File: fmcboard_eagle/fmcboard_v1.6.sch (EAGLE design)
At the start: 231 parts, among them IC1 OPA699ID, IC10 LM358, IC11 7805DT, IC12 SN74AUC2G66DCTR, IC13 SN74AUC2G66DCTR, IC14 SN74AUC2G66DCTR, IC15 SN74AUC2G66DCTR, IC16 DAC7578SPWR, IC17 SN74AUC2G66DCTR, IC18 SN74AUC2G66DCTR, IC19 SN74AUC2G66DCTR, IC2 DAC7578SPWR, IC20 SN74AUC2G66DCTR, IC21 74AUP2GU04GW, IC22 74AUP2GU04GW, IC23 74AUP2GU04GW, IC24 74AUP2GU04GW, IC25 MC7905ACD2TR4G, IC26 AMS1117-1.8, IC29 LM337KVURG3, IC3 LTC6229IMS8E#TRPBF, IC4 OPA695IDR, IC5 LTC6229IMS8E#TRPBF, IC6 OPA695IDR, IC7 OPA699ID, IC8 LM358, IC9 LM358, J1 8pin, J11 4p-2.54, J12 4p-2.54, J13 4p-2.54, J2 ASP-134604-01, J3 4p-2.54, J4 4p-2.54, J5 4p-2.54, J6 4p-2.54, J7 4p-2.54, J8 4p-2.54, J9 8pin, U1 TXS0108EPWR

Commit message: v1.64
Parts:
- R13, R3, R71, R72, R86, R88, R89: LCSC (none) -> C17415
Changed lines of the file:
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@@
 <part name="SUPPLY113" library="supply2" library_urn="urn:adsk.eagle:library:372" deviceset="GND" device=""/>
 <part name="SUPPLY114" library="supply2" library_urn="urn:adsk.eagle:library:372" deviceset="GND" device=""/>
-<part name="R3" library="rcl" library_urn="urn:adsk.eagle:library:334" deviceset="R-US_" device="R0805" package3d_urn="urn:adsk.eagle:package:23553/2" value="10"/>
+<part name="R3" library="rcl" library_urn="urn:adsk.eagle:library:334" deviceset="R-US_" device="R0805" package3d_urn="urn:adsk.eagle:package:23553/2" value="10">
+<spice>
+<pinmapping spiceprefix="R">
+<pinmap gate="G$1" pin="1" pinorder="1"/>
+<pinmap gate="G$1" pin="2" pinorder="2"/>
+</pinmapping>
+</spice>
+<attribute name="LCSC" value="C17415"/>
+</part>
 <part name="SUPPLY18" library="supply2" library_urn="urn:adsk.eagle:library:372" deviceset="GND" device=""/>
-<part name="R13" library="rcl" library_urn="urn:adsk.eagle:library:334" deviceset="R-US_" device="R0805" package3d_urn="urn:adsk.eagle:package:23553/2" value="10"/>
+<part name="R13" library="rcl" library_urn="urn:adsk.eagle:library:334" deviceset="R-US_" device="R0805" package3d_urn="urn:adsk.eagle:package:23553/2" value="10">
+<spice>
+<pinmapping spiceprefix="R">
+<pinmap gate="G$1" pin="1" pinorder="1"/>
+<pinmap gate="G$1" pin="2" pinorder="2"/>
+</pinmapping>
+</spice>
+<attribute name="LCSC" value="C17415"/>
+</part>
 <part name="SUPPLY21" library="supply2" library_urn="urn:adsk.eagle:library:372" deviceset="GND" device=""/>
 <part name="R35" library="rcl" library_urn="urn:adsk.eagle:library:334" deviceset="R-US_" device="R0805" package3d_urn="urn:adsk.eagle:package:23553/2" value="1k"/>
@@
 <part name="J11" library="Seeed-Connector" library_urn="urn:adsk.eagle:library:478" deviceset="DIP-BLACK-FEMALE-HEADER-VERT(4P-2.54)" device="" package3d_urn="urn:adsk.eagle:package:33137/1" value="4p-2.54"/>
 <part name="J13" library="Seeed-Connector" library_urn="urn:adsk.eagle:library:478" deviceset="DIP-BLACK-FEMALE-HEADER-VERT(4P-2.54)" device="" package3d_urn="urn:adsk.eagle:package:33137/1" value="4p-2.54"/>
-<part name="R71" library="rcl" library_urn="urn:adsk.eagle:library:334" deviceset="R-US_" device="R0805" package3d_urn="urn:adsk.eagle:package:23553/2" value="10"/>
-<part name="R72" library="rcl" library_urn="urn:adsk.eagle:library:334" deviceset="R-US_" device="R0805" package3d_urn="urn:adsk.eagle:package:23553/2" value="10"/>
-<part name="R86" library="rcl" library_urn="urn:adsk.eagle:library:334" deviceset="R-US_" device="R0805" package3d_urn="urn:adsk.eagle:package:23553/2" value="10"/>
-<part name="R88" library="rcl" library_urn="urn:adsk.eagle:library:334" deviceset="R-US_" device="R0805" package3d_urn="urn:adsk.eagle:package:23553/2" value="10"/>
+<part name="R71" library="rcl" library_urn="urn:adsk.eagle:library:334" deviceset="R-US_" device="R0805" package3d_urn="urn:adsk.eagle:package:23553/2" value="10">
+<spice>
+<pinmapping spiceprefix="R">
+<pinmap gate="G$1" pin="1" pinorder="1"/>
+<pinmap gate="G$1" pin="2" pinorder="2"/>
+</pinmapping>
+</spice>
+<attribute name="LCSC" value="C17415"/>
+</part>
+<part name="R72" library="rcl" library_urn="urn:adsk.eagle:library:334" deviceset="R-US_" device="R0805" package3d_urn="urn:adsk.eagle:package:23553/2" value="10">
+<spice>
+<pinmapping spiceprefix="R">
+<pinmap gate="G$1" pin="1" pinorder="1"/>
+<pinmap gate="G$1" pin="2" pinorder="2"/>
+</pinmapping>
+</spice>
+<attribute name="LCSC" value="C17415"/>
+</part>
+<part name="R86" library="rcl" library_urn="urn:adsk.eagle:library:334" deviceset="R-US_" device="R0805" package3d_urn="urn:adsk.eagle:package:23553/2" value="10">
+<spice>
+<pinmapping spiceprefix="R">
+<pinmap gate="G$1" pin="1" pinorder="1"/>
+<pinmap gate="G$1" pin="2" pinorder="2"/>
+</pinmapping>
+</spice>
+<attribute name="LCSC" value="C17415"/>
+</part>
+<part name="R88" library="rcl" library_urn="urn:adsk.eagle:library:334" deviceset="R-US_" device="R0805" package3d_urn="urn:adsk.eagle:package:23553/2" value="10">
+<spice>
+<pinmapping spiceprefix="R">
+<pinmap gate="G$1" pin="1" pinorder="1"/>
+<pinmap gate="G$1" pin="2" pinorder="2"/>
+</pinmapping>
+</spice>
+<attribute name="LCSC" value="C17415"/>
+</part>
 <part name="J5" library="Seeed-Connector" library_urn="urn:adsk.eagle:library:478" deviceset="DIP-BLACK-FEMALE-HEADER-VERT(4P-2.54)" device="" package3d_urn="urn:adsk.eagle:package:33137/1" value="4p-2.54"/>
-<part name="R89" library="rcl" library_urn="urn:adsk.eagle:library:334" deviceset="R-US_" device="R0805" package3d_urn="urn:adsk.eagle:package:23553/2" value="10"/>
+<part name="R89" library="rcl" library_urn="urn:adsk.eagle:library:334" deviceset="R-US_" device="R0805" package3d_urn="urn:adsk.eagle:package:23553/2" value="10">
+<spice>
+<pinmapping spiceprefix="R">
+<pinmap gate="G$1" pin="1" pinorder="1"/>
+<pinmap gate="G$1" pin="2" pinorder="2"/>
+</pinmapping>
+</spice>
+<attribute name="LCSC" value="C17415"/>
+</part>
 <part name="C95" library="SparkFun-Passives" deviceset="CAP_POL" device="SMD" value="100uF">
 <attribute name="LCSC" value="C7230"/>
@@
 <attribute name="NAME" x="166.5986" y="77.47" size="1.778" layer="95" rot="R270"/>
 <attribute name="VALUE" x="161.798" y="77.47" size="1.778" layer="96" rot="R270"/>
+<attribute name="LCSC" x="165.1" y="76.2" size="1.778" layer="96" rot="R270" display="off"/>
 </instance>
 <instance part="SUPPLY18" gate="GND" x="165.1" y="68.58" smashed="yes"/>
@@
 <attribute name="NAME" x="161.5186" y="118.11" size="1.778" layer="95" rot="R270"/>
 <attribute name="VALUE" x="156.718" y="118.11" size="1.778" layer="96" rot="R270"/>
+<attribute name="LCSC" x="160.02" y="116.84" size="1.778" layer="96" rot="R270" display="off"/>
 </instance>
 <instance part="SUPPLY21" gate="GND" x="160.02" y="109.22" smashed="yes"/>
@@
 <attribute name="NAME" x="278.13" y="49.3014" size="1.778" layer="95" rot="R180"/>
 <attribute name="VALUE" x="278.13" y="46.482" size="1.778" layer="96" rot="R180"/>
+<attribute name="LCSC" x="276.86" y="43.18" size="1.778" layer="96" rot="R180" display="off"/>
 </instance>
 <instance part="R72" gate="G$1" x="276.86" y="38.1" smashed="yes" rot="R180">
 <attribute name="NAME" x="278.13" y="36.6014" size="1.778" layer="95" rot="R180"/>
 <attribute name="VALUE" x="278.13" y="33.782" size="1.778" layer="96" rot="R180"/>
+<attribute name="LCSC" x="276.86" y="38.1" size="1.778" layer="96" rot="R180" display="off"/>
 </instance>
 <instance part="R86" gate="G$1" x="276.86" y="15.24" smashed="yes" rot="R180">
 <attribute name="NAME" x="278.13" y="13.7414" size="1.778" layer="95" rot="R180"/>
 <attribute name="VALUE" x="278.13" y="10.922" size="1.778" layer="96" rot="R180"/>
+<attribute name="LCSC" x="276.86" y="15.24" size="1.778" layer="96" rot="R180" display="off"/>
 </instance>
 <instance part="R88" gate="G$1" x="109.22" y="30.48" smashed="yes" rot="R180">
 <attribute name="NAME" x="113.03" y="28.9814" size="1.778" layer="95" rot="R180"/>
 <attribute name="VALUE" x="113.03" y="33.782" size="1.778" layer="96" rot="R180"/>
+<attribute name="LCSC" x="109.22" y="30.48" size="1.778" layer="96" rot="R180" display="off"/>
 </instance>
 <instance part="J5" gate="G$1" x="289.56" y="16.51" smashed="yes"/>
@@
 <attribute name="NAME" x="278.13" y="26.4414" size="1.778" layer="95" rot="R180"/>
 <attribute name="VALUE" x="278.13" y="23.622" size="1.778" layer="96" rot="R180"/>
+<attribute name="LCSC" x="276.86" y="20.32" size="1.778" layer="96" rot="R180" display="off"/>
 </instance>
 <instance part="IC1" gate="G$1" x="175.26" y="88.9" smashed="yes">

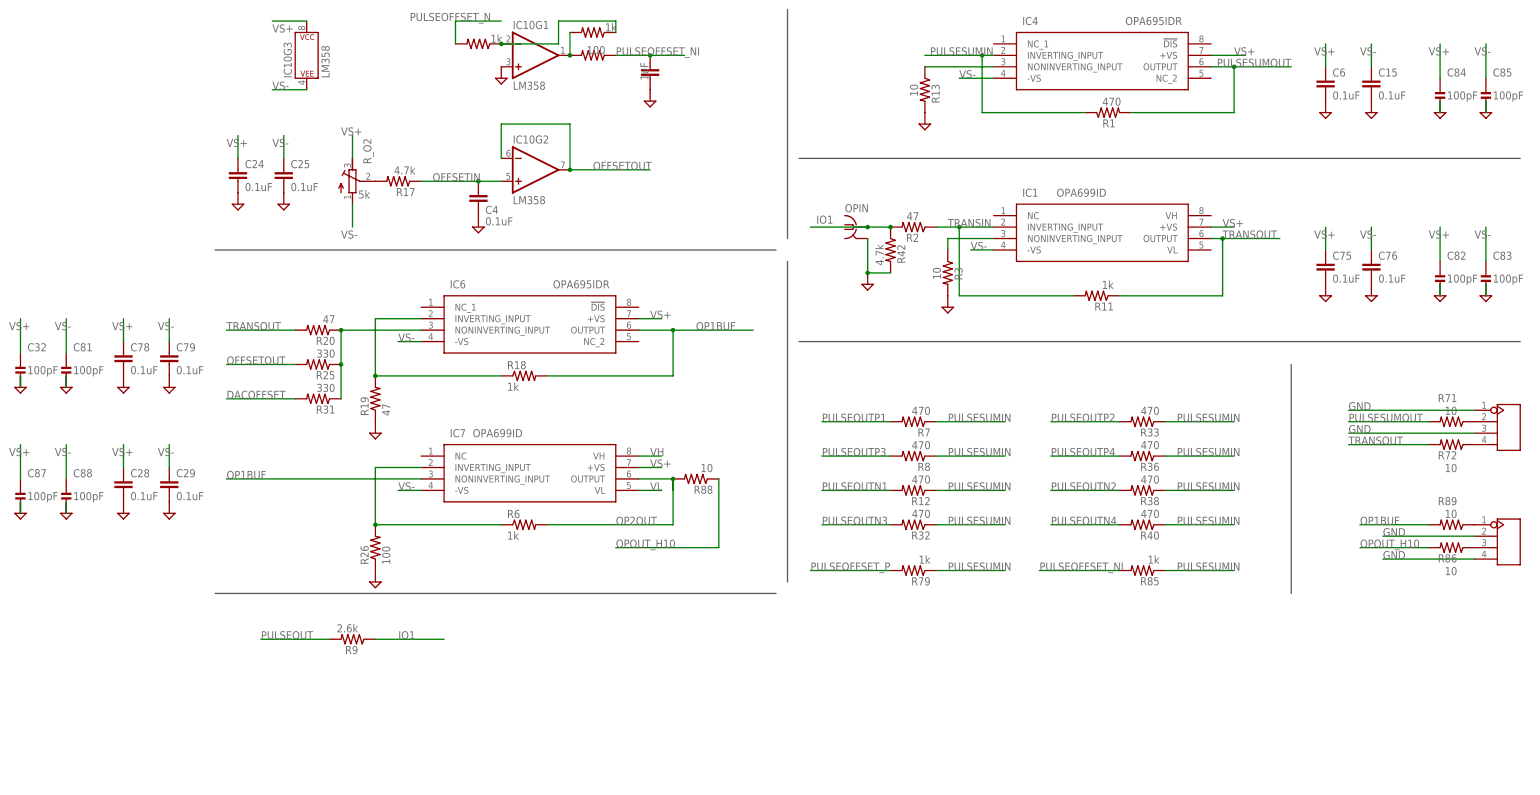
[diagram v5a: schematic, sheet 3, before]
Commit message: v1.65 4.7k -> 100 for input termination 2.6k -> 1-3k for test resistor 100 to gnd on h10/11 h10 -> 10 ohm -> h11 h27/28 -> h28/29
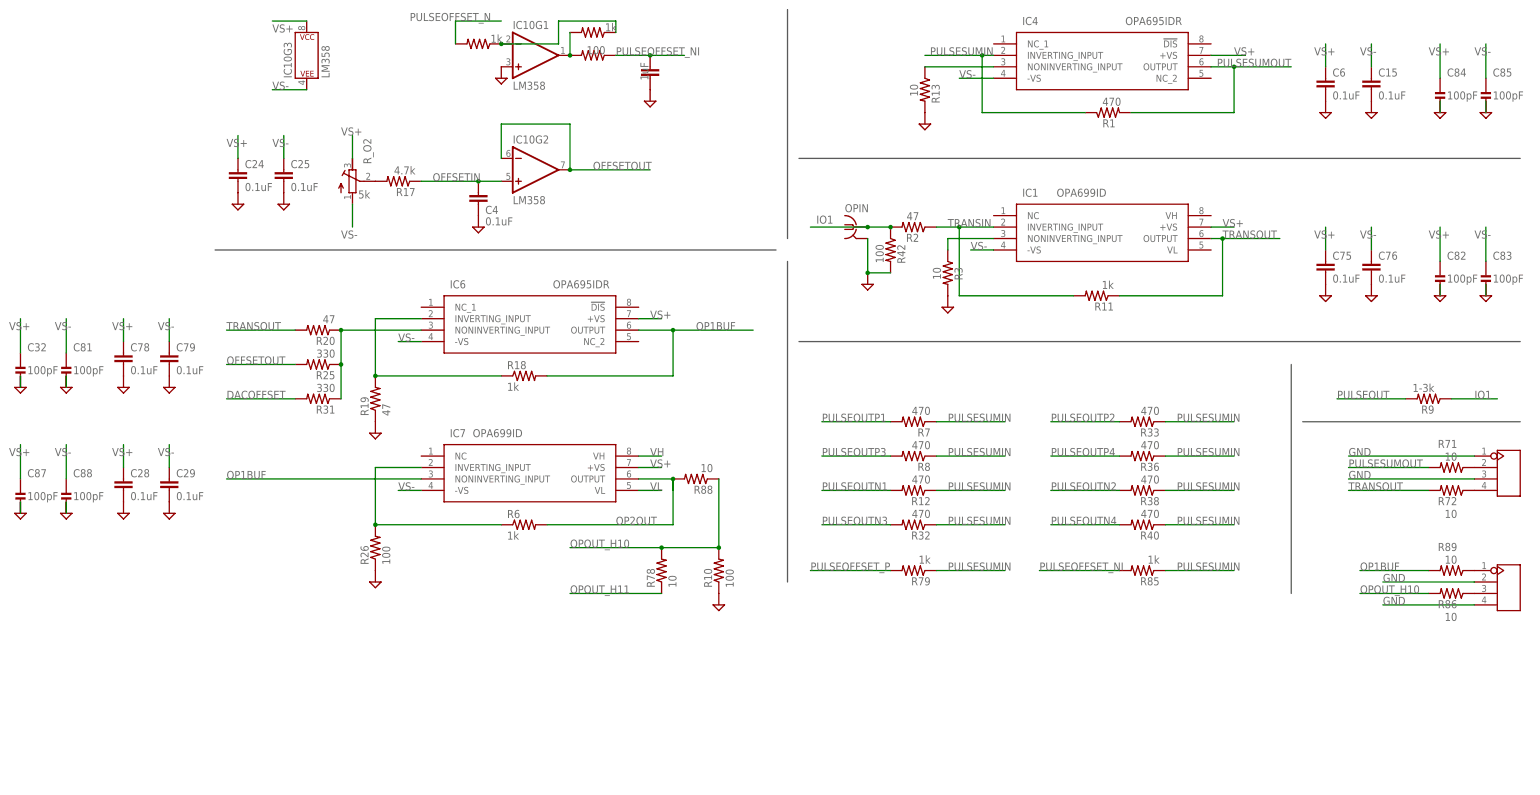
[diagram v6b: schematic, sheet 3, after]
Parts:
- added R10: 100, rcl:R-US_R0805
- added R78: 10, rcl:R-US_R0805
- R42: value 4.7k -> 100
- R9: value 2.6k -> 1-3k
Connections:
- removed net H27: J2.H28, SV2.1
- new net H29: J2.H29, SV2.2
- net GND: now also R10.1
- net H28: now also J2.H28, SV2.1; no longer J2.H29, SV2.2
- net OPOUT_H10: now also R10.2, R78.2
- net OPOUT_H11: now also R78.1
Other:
- moved on the sheet: R71, R72, R86, R89, R9

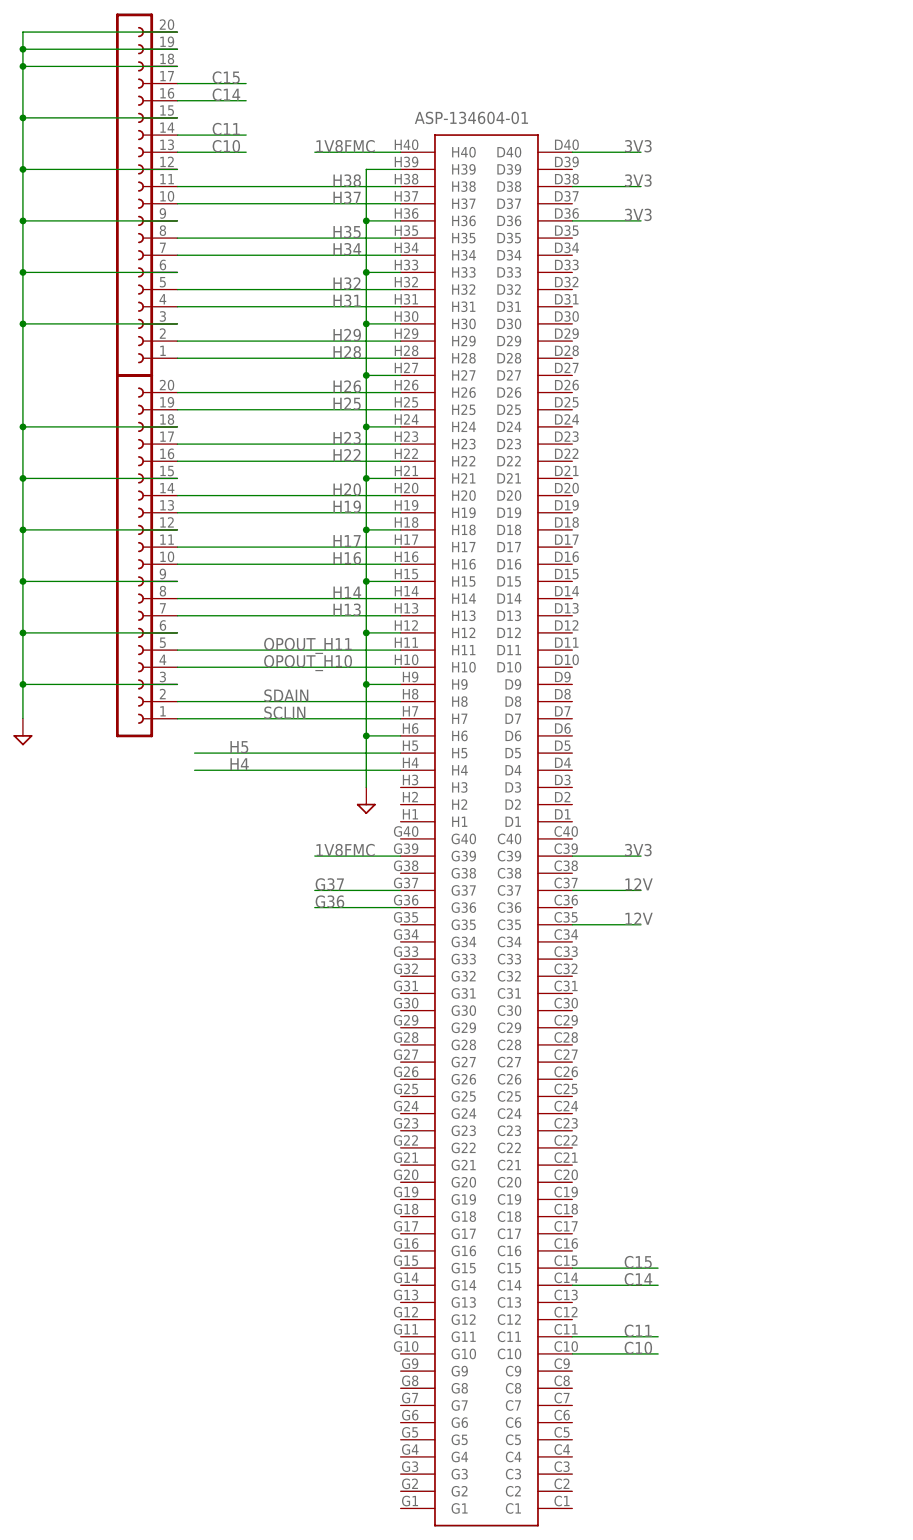
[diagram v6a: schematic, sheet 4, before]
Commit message: v1.65 add gnds to fmc and extra C connections
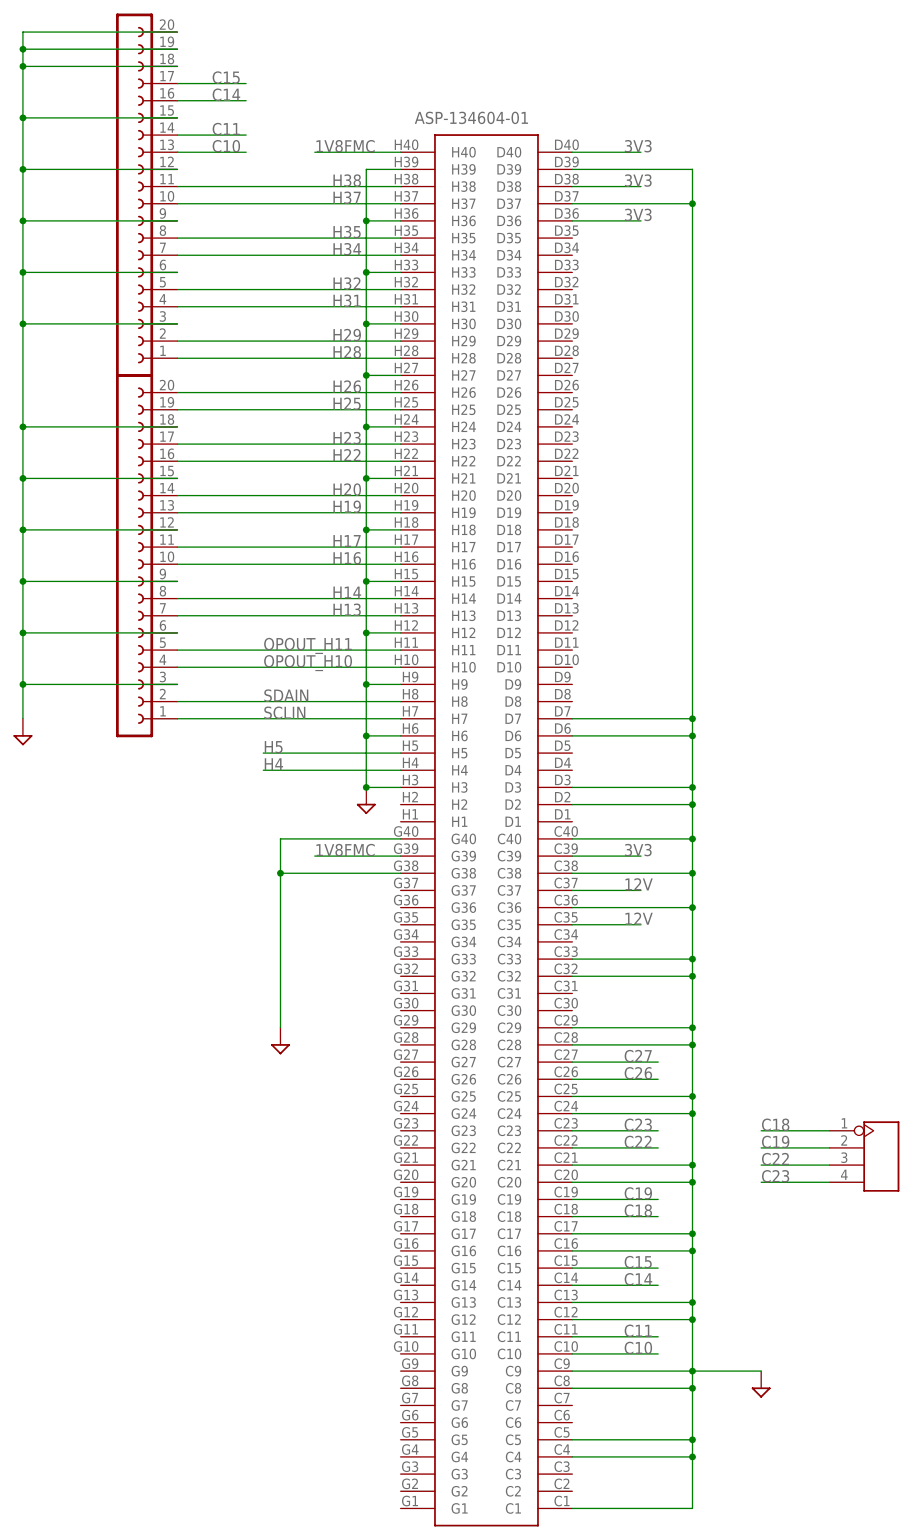
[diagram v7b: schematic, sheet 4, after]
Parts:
- added J10: 4p-2.54, Seeed-Connector:DIP-BLACK-FEMALE-HEADER-VERT(4P-2.54)
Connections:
- net AR_G36 renamed AR_C26
- net AR_G37 renamed AR_C27
- removed net G36: J2.G36, U1.A4
- removed net G37: J2.G37, U1.A5
- new net C18: J10.P$1, J2.C18
- new net C19: J10.P$2, J2.C19
- new net C22: J10.P$3, J2.C22
- new net C23: J10.P$4, J2.C23
- new net C26: J2.C26, U1.A4
- new net C27: J2.C27, U1.A5
- net GND: now also J2.C1, J2.C12, J2.C13, J2.C16, J2.C17, J2.C20, J2.C21, J2.C24, J2.C25, J2.C28, J2.C29, J2.C32, J2.C33, J2.C36, J2.C38, J2.C4, J2.C40, J2.C5, J2.C8, J2.C9, J2.D2, J2.D3, J2.D37, J2.D39, J2.D6, J2.D7, J2.G38, J2.G40, J2.H3
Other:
- note added: "extra"
